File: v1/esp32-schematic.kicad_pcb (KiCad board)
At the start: 2 copper layers, 46 parts, among them J1 GN-2630G, J10 Screw_Terminal_01x04, J11 Screw_Terminal_01x04, J12 Screw_Terminal_01x04, J13 Screw_Terminal_01x04, J15 POWER, J2 Jumper, J3 Micro_SD_Card, J4 Screw_Terminal_01x04, J5 Screw_Terminal_01x04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

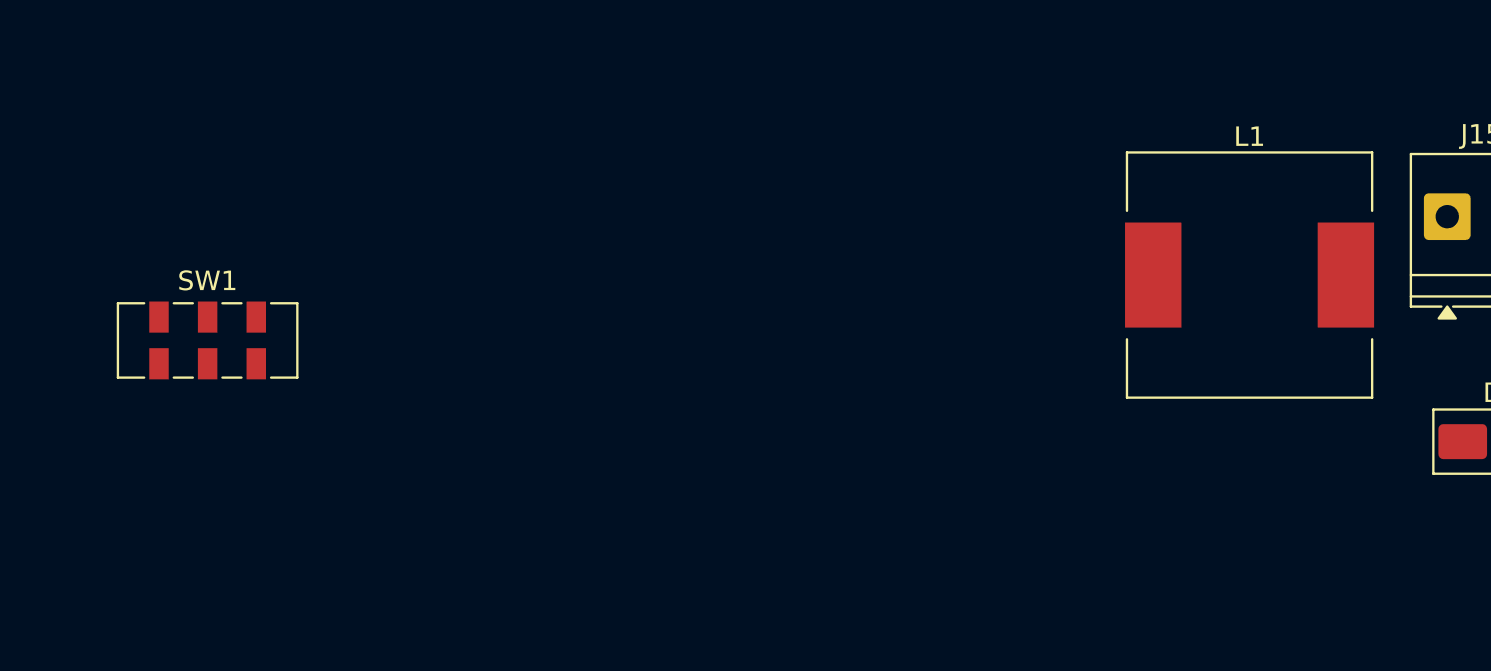
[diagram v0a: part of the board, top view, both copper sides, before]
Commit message: Reorganisation of the project, the v1 will be the test prototype and the v2 will be implementing the devices on the board directly. Also the libraries have been reorganised, each version will share all the libraries, this way we can stop importing the same components over and over. Also a recommended command to add to the source in case you are using linux, see the README
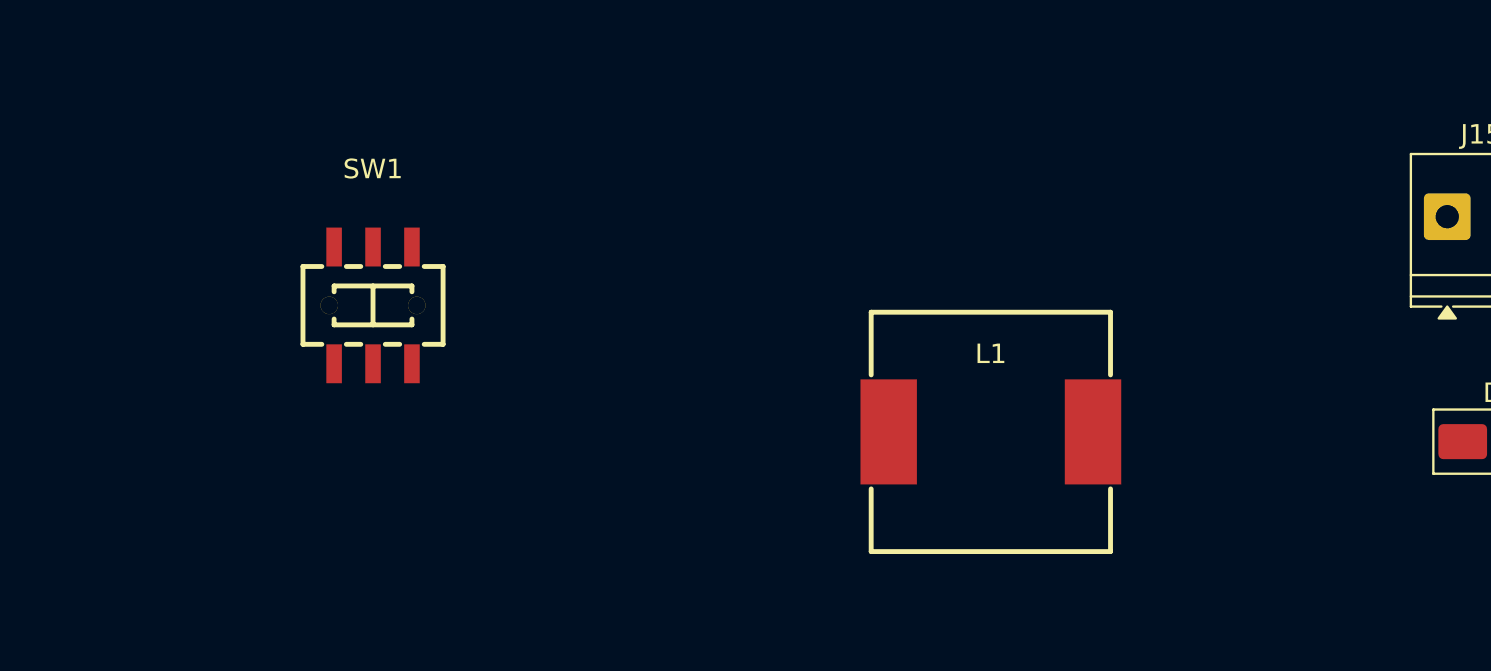
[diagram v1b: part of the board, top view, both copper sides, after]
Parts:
- L1: value 68uH -> SMDRI127-680MT; footprint Inductor_SMD:L_12x12mm_H6mm -> easyeda2kicad:IND-SMD_L12.3-W12.3_SMDRI127
- SW1: value SW_SPDT -> MS-22D28-G020; footprint Button_Switch_SMD:SW_DPDT_CK_JS202011JCQN -> easyeda2kicad:SW-SMD_MS-22D28-G020
- moved L1 15.5 mm to (192.2, 141.0)
- moved SW1 8.69 mm to (160.5, 134.5)
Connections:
- C10 pad 2: GND -> Net-(D1-A)
- C11 pad 1: Net-(SW1-B) -> Net-(C11-Pad1)
- C11 pad 2: GND -> Net-(D1-A)
- C12 pad 2: Net-(SW1-B) -> Net-(C11-Pad1)
- D1 pad 2: GND -> Net-(D1-A)
- J15 pad 2: GND -> Net-(D1-A)
- L1 pad 2: Net-(SW1-B) -> Net-(C11-Pad1)
- R12 pad 1: Net-(SW1-B) -> Net-(C11-Pad1)
- SW1 pad 1: +5V -> Net-(C11-Pad1)
- SW1 pad 2: Net-(SW1-B) -> Net-(D1-A)
- SW1 pad 4: (no net) -> +5V
- SW1 pad 5: (no net) -> GND
- SW1 pad 6: (no net) -> unconnected-(SW1-Pad6)
- U5 pad 3: GND -> Net-(D1-A)
- U5 pad 5: GND -> Net-(D1-A)

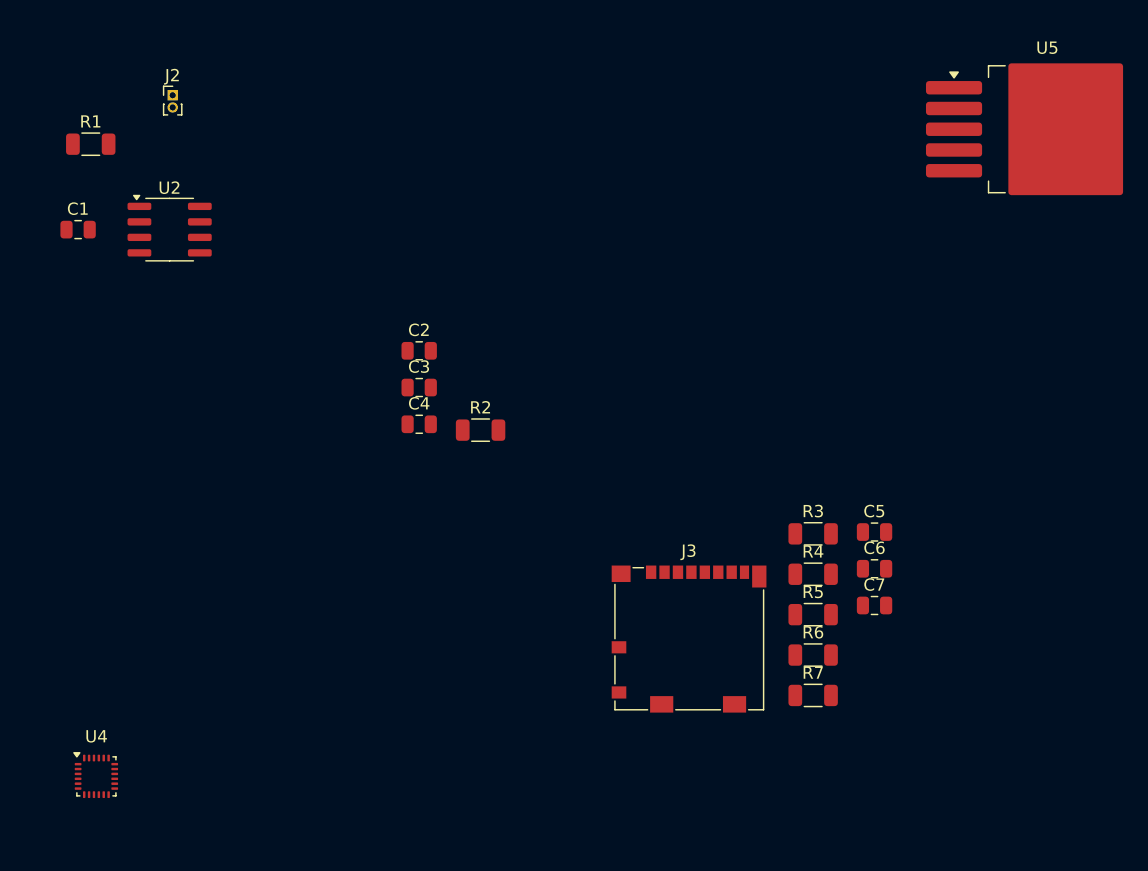
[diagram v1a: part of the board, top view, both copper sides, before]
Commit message: external power supply entry added, and todo list updated
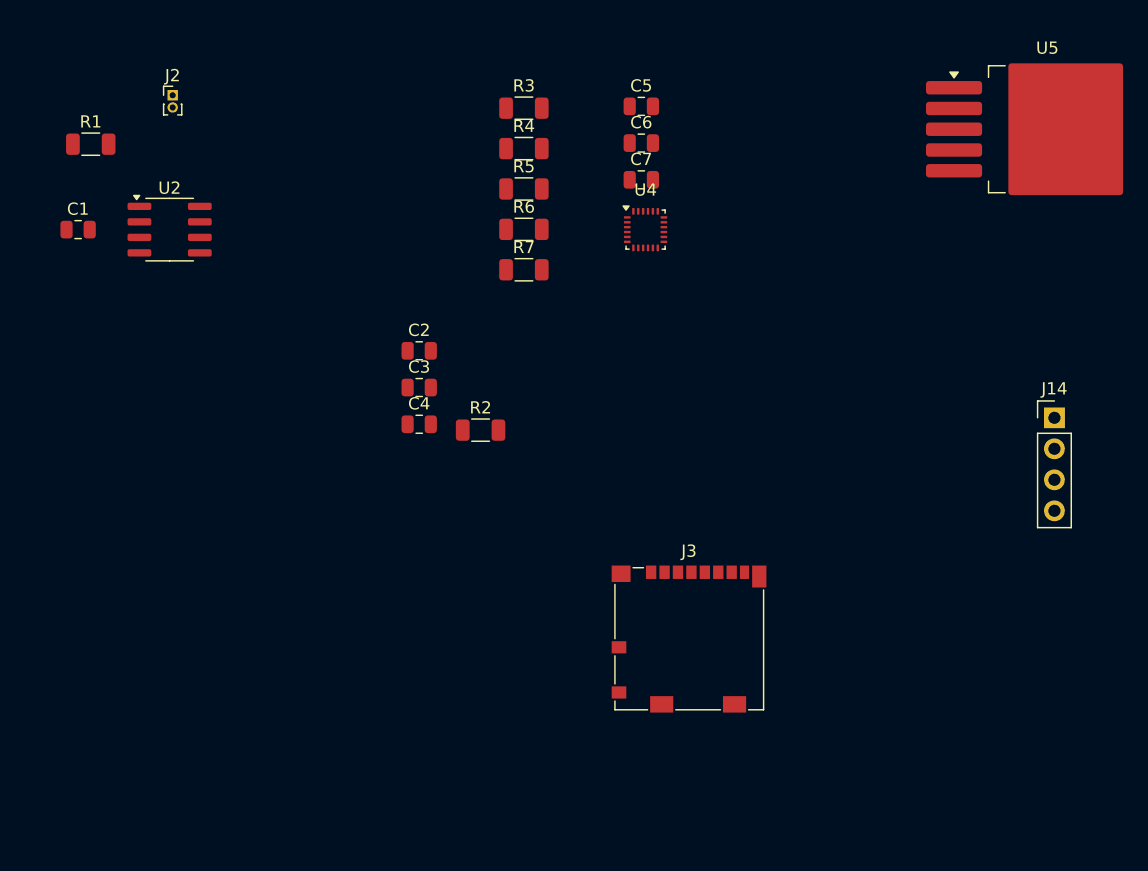
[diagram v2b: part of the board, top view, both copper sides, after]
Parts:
- added J14: External Voltage Regulator, Connector_PinHeader_2.54mm:PinHeader_1x04_P2.54mm_Vertical, F.Cu at (191.0, 61.9)
- moved U4 63.5 mm to (157.5, 46.5)
- moved R3 42.2 mm to (147.5, 36.5)
- moved R6 42.2 mm to (147.5, 46.5)
- moved R7 42.2 mm to (147.5, 49.8)
- moved R4 42.2 mm to (147.5, 39.9)
- moved R5 42.2 mm to (147.5, 43.2)
- moved C5 39.8 mm to (157.2, 36.4)
- moved C6 39.8 mm to (157.2, 39.4)
- moved C7 39.8 mm to (157.2, 42.4)
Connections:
- SW1 pad 3: unconnected-(SW1-Pad3) -> Net-(J14-Pin_3)
